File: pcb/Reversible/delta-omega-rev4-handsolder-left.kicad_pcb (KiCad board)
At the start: 2 copper layers, 107.4 x 81.2 mm, 52 parts, among them SW16 ULP_SW

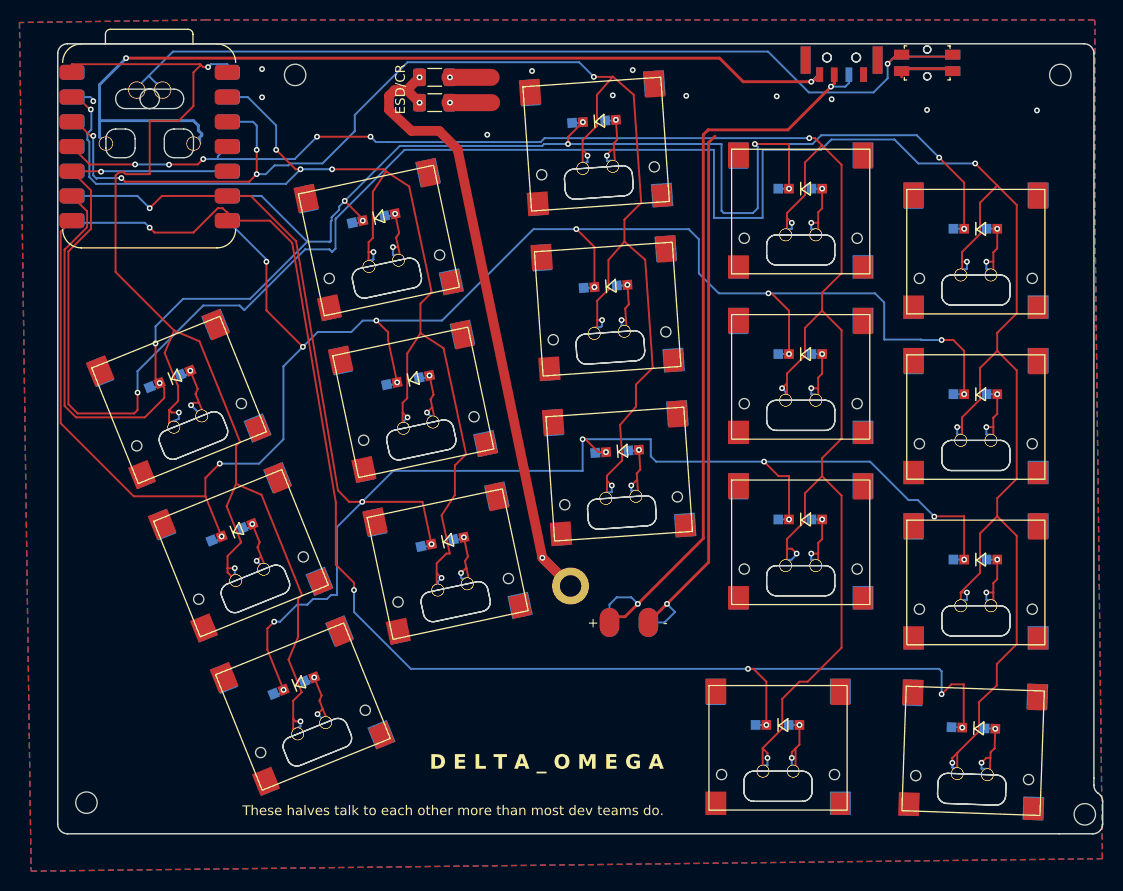
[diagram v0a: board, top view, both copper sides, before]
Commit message: Update the copper filled zone and some track
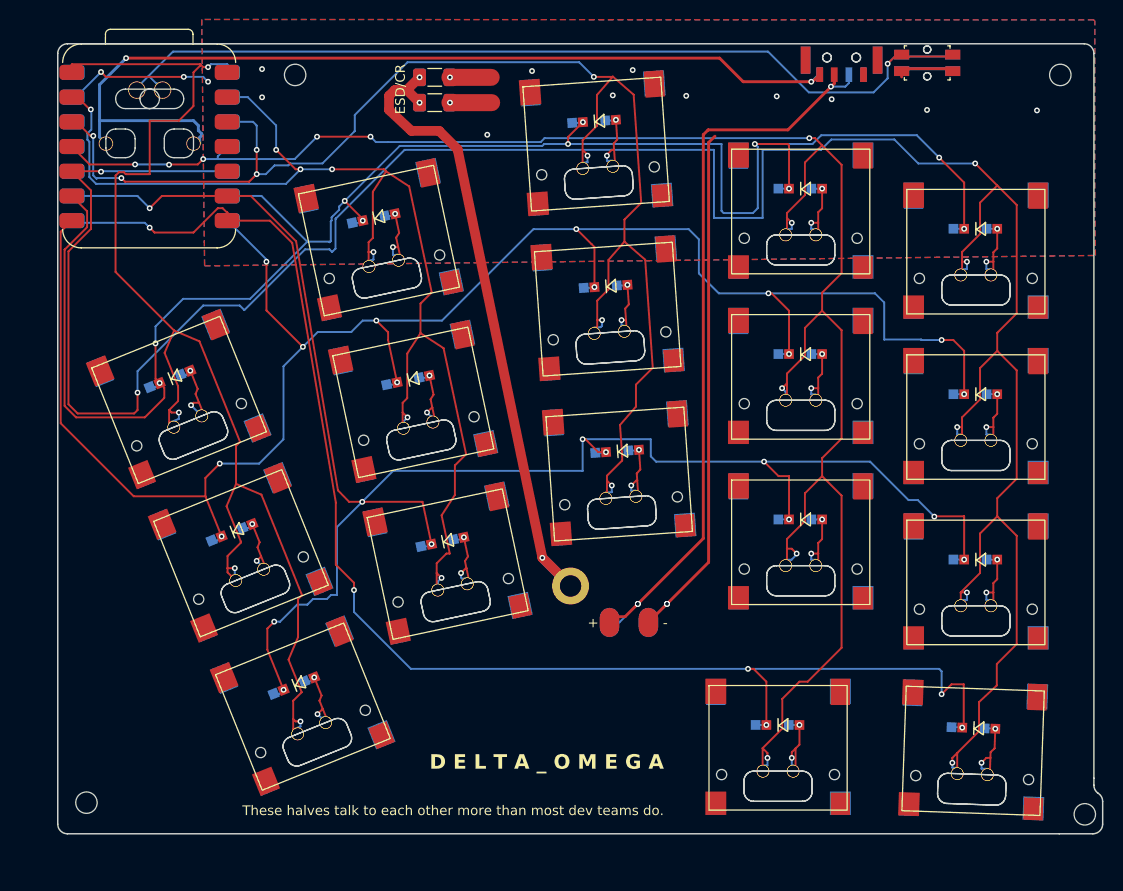
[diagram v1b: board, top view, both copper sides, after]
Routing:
- net L_GND: track 79.6 -> 91.0 mm, vias 15 -> 18
- net L_RAW: track 79.8 -> 78.2 mm, vias 2 -> 3
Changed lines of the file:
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@@
 	)
 	(via
+		(at 80.675 90.175)
+		(size 0.6)
+		(drill 0.3)
+		(layers "F.Cu" "B.Cu")
+		(net "L_RAW")
+	)
+	(via
 		(at 100.525 37)
 		(size 0.6)
@@
 	)
 	(segment
-		(start 102.366075 35.774592)
-		(end 102.366075 36.633925)
+		(start 78.768798 92.081202)
+		(end 80.675 90.175)
 		(width 0.2)
 		(layer "B.Cu")
@@
 	)
 	(segment
-		(start 78.5 89.5)
-		(end 80 89.5)
+		(start 102.366075 35.774592)
+		(end 102.366075 36.633925)
 		(width 0.2)
 		(layer "B.Cu")
@@
 	)
 	(segment
-		(start 77.761013 90.238987)
-		(end 78.5 89.5)
+		(start 77.761013 92.081202)
+		(end 78.768798 92.081202)
 		(width 0.2)
 		(layer "B.Cu")
@@
 	)
 	(segment
-		(start 77.761013 92.081202)
-		(end 77.761013 90.238987)
-		(width 0.2)
-		(layer "B.Cu")
-		(net "L_RAW")
-	)
-	(segment
-		(start 80 89.5)
-		(end 80.675 90.175)
-		(width 0.2)
-		(layer "B.Cu")
-		(net "L_RAW")
-	)
-	(segment
 		(start 89.075 34.075)
 		(end 28.075 34.075)
@@
 	)
 	(segment
+		(start 25.5 35.5)
+		(end 26 36)
+		(width 0.2)
+		(layer "F.Cu")
+		(net "L_GND")
+	)
+	(segment
 		(start 81.761013 92.081202)
 		(end 83.671107 90.171107)
@@
 		(net "L_GND")
 	)
+	(segment
+		(start 26 36)
+		(end 34 36)
+		(width 0.2)
+		(layer "F.Cu")
+		(net "L_GND")
+	)
 	(via
 		(at 110.4 39.4)
@@
 	)
 	(via
+		(at 25.5 35.5)
+		(size 0.6)
+		(drill 0.3)
+		(layers "F.Cu" "B.Cu")
+		(net "L_GND")
+	)
+	(via
 		(at 65.2 41.95)
 		(size 0.6)
@@
 	)
 	(via
+		(at 36.5 36.5)
+		(size 0.6)
+		(drill 0.3)
+		(layers "F.Cu" "B.Cu")
+		(net "L_GND")
+	)
+	(via
 		(at 85.65 37.95)
 		(size 0.6)
@@
 	)
 	(via
-		(at 24.7 38.5)
-		(size 0.6)
-		(drill 0.3)
-		(layers "F.Cu" "B.Cu")
-		(net "L_GND")
-	)
-	(via
 		(at 121.7 39.45)
 		(size 0.6)
@@
 	)
 	(via
+		(at 83.671107 90.171107)
+		(size 0.6)
+		(drill 0.3)
+		(layers "F.Cu" "B.Cu")
+		(net "L_GND")
+	)
+	(via
 		(at 69.8 35.4)
 		(size 0.6)
@@
 	)
 	(via
+		(at 34 36)
+		(size 0.6)
+		(drill 0.3)
+		(layers "F.Cu" "B.Cu")
+		(net "L_GND")
+	)
+	(via
 		(at 42.05 35.2)
 		(size 0.6)
@@
 	)
 	(segment
-		(start 24.7 38.36)
-		(end 24.42 38.08)
+		(start 22.545 38.08)
+		(end 22.92 38.08)
+		(width 0.2)
+		(layer "B.Cu")
+		(net "L_GND")
+	)
+	(segment
+		(start 81.761013 92.081202)
+		(end 83.671107 90.171108)
 		(width 0.2)
 		(layer "B.Cu")
@@
 	)
 	(segment
-		(start 24.42 38.08)
-		(end 22.545 38.08)
+		(start 36 36)
+		(end 36.5 36.5)
 		(width 0.2)
 		(layer "B.Cu")
@@
 	)
 	(segment
-		(start 108.041075 35.164592)
-		(end 107.991075 35.214592)
-		(width 0.3)
-		(layer "B.Cu")
-		(net "L_GND")
-	)
-	(segment
-		(start 83.418798 92.081202)
-		(end 84.5 91)
+		(start 22.92 38.08)
+		(end 25.5 35.5)
 		(width 0.2)
 		(layer "B.Cu")
@@
 	)
 	(segment
-		(start 84.5 91)
+		(start 83.671107 90.171108)
 		(end 83.671107 90.171107)
 		(width 0.2)
@@
 	)
 	(segment
-		(start 81.761013 92.081202)
-		(end 83.418798 92.081202)
-		(width 0.2)
+		(start 108.041075 35.164592)
+		(end 107.991075 35.214592)
+		(width 0.3)
 		(layer "B.Cu")
 		(net "L_GND")
 	)
 	(segment
-		(start 24.7 38.5)
-		(end 24.7 38.36)
+		(start 34 36)
+		(end 36 36)
 		(width 0.2)
 		(layer "B.Cu")
@@
 		(polygon
 			(pts
-				(xy 17.11429 30.414169) (xy 18.312201 117.641151) (xy 128.427353 116.361876) (xy 127.65 49.45) (xy 127.65 30.25)
-				(xy 127.55 30.15) (xy 36.35 30.15)
+				(xy 35.849632 30.099406) (xy 36.144834 55.425864) (xy 127.707026 54.358626) (xy 127.65 49.45) (xy 127.65 30.25)
+				(xy 127.55 30.15) (xy 35.849139 30.099406)
 			)
 		)

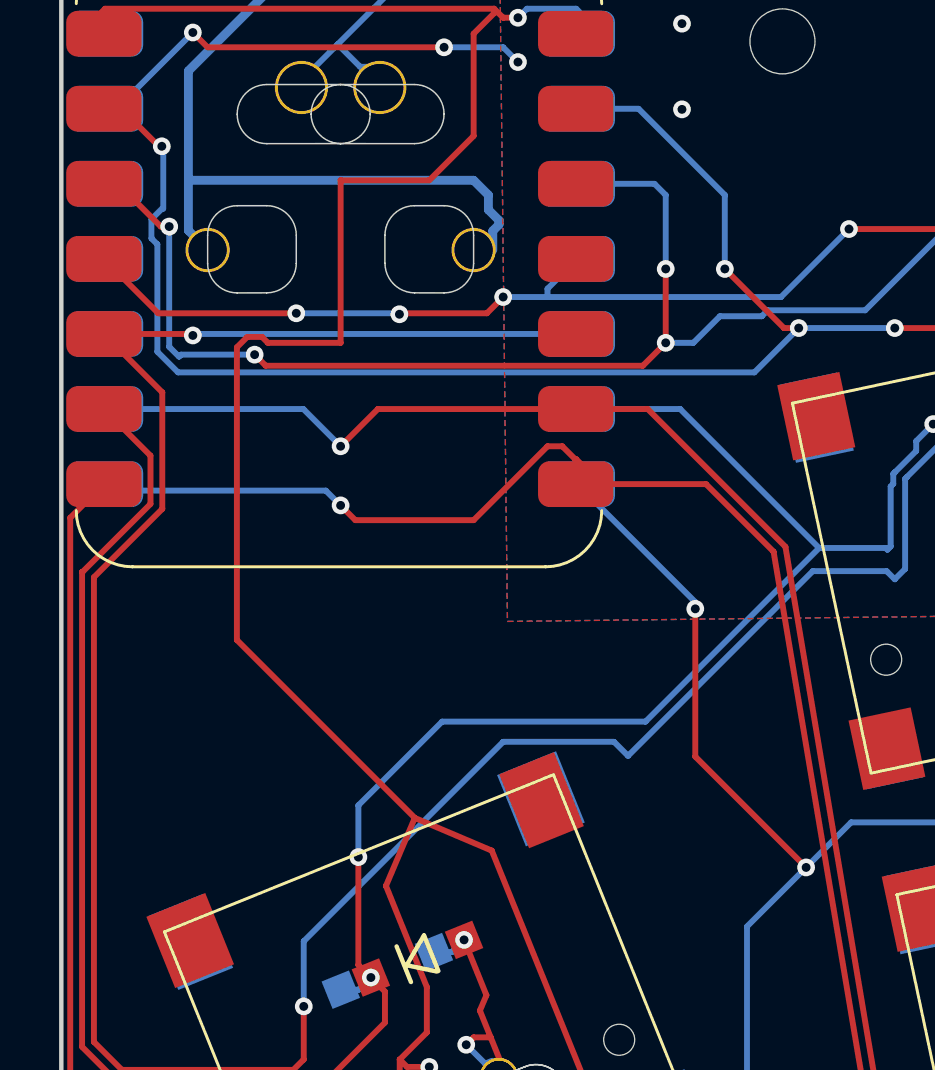
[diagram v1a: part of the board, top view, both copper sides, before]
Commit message: fix traces under controller
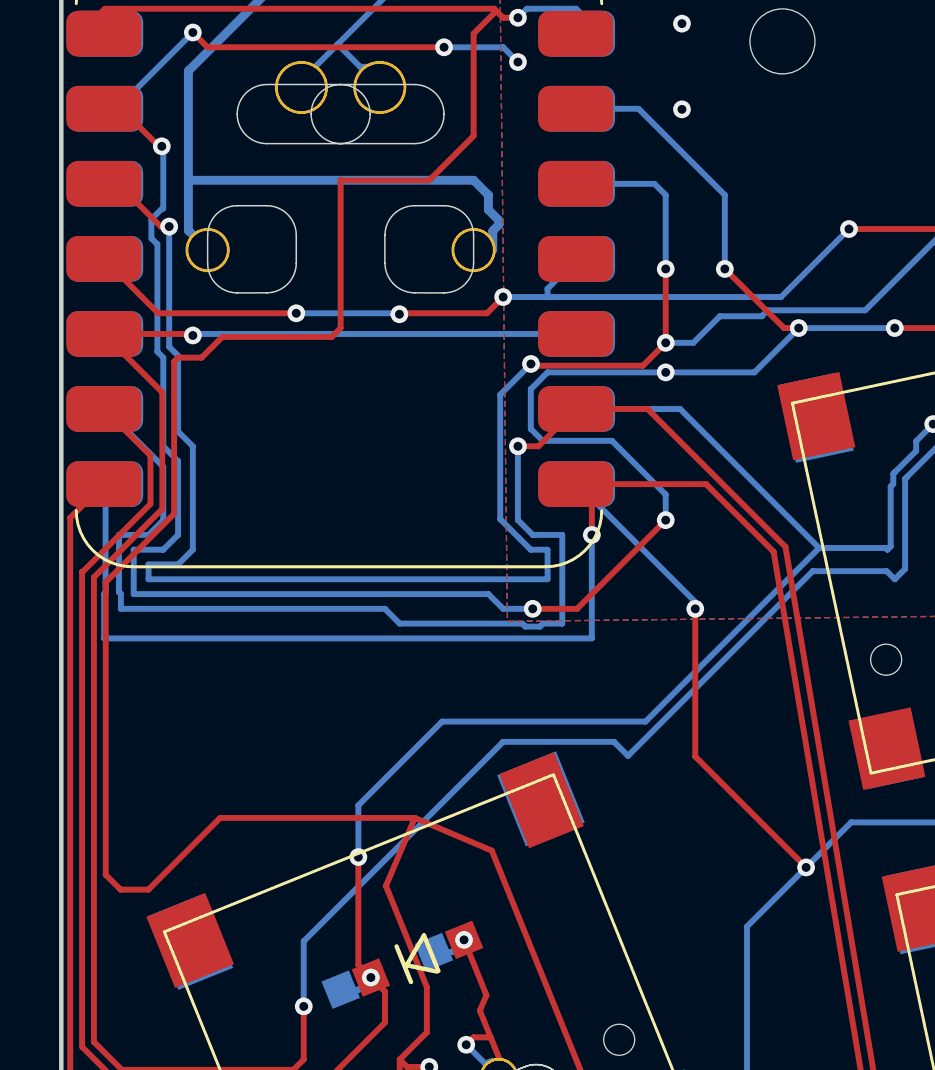
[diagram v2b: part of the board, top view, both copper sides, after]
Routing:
- net L_C2: track 125.6 -> 149.8 mm, vias 7 -> 10
- net L_C3: track 149.5 -> 168.6 mm
- net L_R3: track 182.4 -> 199.2 mm
- net L_C1: track 130.7 -> 144.1 mm
- net L_R4: track 145.9 -> 155.5 mm
